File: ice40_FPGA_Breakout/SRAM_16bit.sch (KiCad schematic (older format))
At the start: 0 parts

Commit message: Added SO-DIMM header, ice40 IO and FTDI power
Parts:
- added C? (x3): C, symbol C
- added R? (x4): 10K, symbol R
- added U? (x3): iCE40HX8_CT256, symbol iCE40HX8_CT256
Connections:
- new net 3V3_REF_IN: C?.1, C?.1, C?.1, R?.1, R?.1, R?.1, R?.1, U?.N13 (VCC_SPI)
- new net FPGA_SPI_CLK: R?.2, U?.R11 (IOB_107_SCK)
- new net FPGA_SPI_CSN: R?.2, U?.R12 (IOB_108_SS)
- new net FPGA_SPI_SDI: R?.2, U?.P11 (IOB_106_SDI)
- new net FPGA_SPI_SDO: R?.2, U?.P12 (IOB_105_SDO)
- new net GND: C?.2, C?.2, C?.2
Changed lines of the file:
@@
 $Descr A4 11693 8268
 encoding utf-8
-Sheet 1 7
+Sheet 3 7
 Title ""
 Date ""
@@
 Comment4 ""
 $EndDescr
+$Comp
+L iCE40HX8_CT256 U?
+U 6 1 5A3EF3FF
+P 8250 5550
+AR Path="/5A0778ED/5A3EF3FF" Ref="U?"  Part="6"
+AR Path="/5A07796D/5A3EF3FF" Ref="U?"  Part="6"
+F 0 "U?" H 8350 5650 60  0000 C CNN
+F 1 "iCE40HX8_CT256" H 8950 5500 60  0000 C CNN
+F 2 "" H 8250 5550 60  0001 C CNN
+F 3 "" H 8250 5550 60  0001 C CNN
+	6    8250 5550
+	1    0    0    -1
+$EndComp
+Text HLabel 7450 5700 0    60   Input ~ 0
+FPGA_SPI_SDO
+Text HLabel 7450 5800 0    60   Input ~ 0
+FPGA_SPI_SDI
+Text HLabel 7450 5900 0    60   Input ~ 0
+FPGA_SPI_CLK
+Text HLabel 10400 5700 2    60   Input ~ 0
+FPGA_SPI_CSN
+Wire Wire Line
+	9900 5800 10050 5800
+Wire Wire Line
+	10050 5800 10250 5800
+$Comp
+L iCE40HX8_CT256 U?
+U 2 1 5A3F10D7
+P 2200 650
+F 0 "U?" H 2300 750 60  0000 C CNN
+F 1 "iCE40HX8_CT256" H 2900 550 60  0000 C CNN
+F 2 "" H 2200 650 60  0001 C CNN
+F 3 "" H 2200 650 60  0001 C CNN
+	2    2200 650
+	1    0    0    -1
+$EndComp
+$Comp
+L iCE40HX8_CT256 U?
+U 3 1 5A3F1322
+P 2200 4300
+F 0 "U?" H 2300 4400 60  0000 C CNN
+F 1 "iCE40HX8_CT256" H 2900 4200 60  0000 C CNN
+F 2 "" H 2200 4300 60  0001 C CNN
+F 3 "" H 2200 4300 60  0001 C CNN
+	3    2200 4300
+	1    0    0    -1
+$EndComp
+Wire Wire Line
+	7450 5700 7600 5700
+Wire Wire Line
+	7600 5700 8050 5700
+Wire Wire Line
+	7450 5800 7750 5800
+Wire Wire Line
+	7750 5800 8050 5800
+Wire Wire Line
+	7450 5900 7900 5900
+Wire Wire Line
+	7900 5900 8050 5900
+Wire Wire Line
+	9900 5700 10050 5700
+Wire Wire Line
+	10050 5700 10400 5700
+$Comp
+L R R?
+U 1 1 5A3F7BB8
+P 7750 5400
+F 0 "R?" V 7830 5400 50  0000 C CNN
+F 1 "10K" V 7750 5400 50  0000 C CNN
+F 2 "" V 7680 5400 50  0001 C CNN
+F 3 "" H 7750 5400 50  0001 C CNN
+	1    7750 5400
+	1    0    0    -1
+$EndComp
+$Comp
+L R R?
+U 1 1 5A3F7C81
+P 7900 5400
+F 0 "R?" V 7980 5400 50  0000 C CNN
+F 1 "10K" V 7900 5400 50  0000 C CNN
+F 2 "" V 7830 5400 50  0001 C CNN
+F 3 "" H 7900 5400 50  0001 C CNN
+	1    7900 5400
+	1    0    0    -1
+$EndComp
+$Comp
+L R R?
+U 1 1 5A3F7CA8
+P 7600 5400
+F 0 "R?" V 7680 5400 50  0000 C CNN
+F 1 "10K" V 7600 5400 50  0000 C CNN
+F 2 "" V 7530 5400 50  0001 C CNN
+F 3 "" H 7600 5400 50  0001 C CNN
+	1    7600 5400
+	1    0    0    -1
+$EndComp
+Wire Wire Line
+	7600 5550 7600 5700
+Connection ~ 7600 5700
+Wire Wire Line
+	7750 5550 7750 5800
+Connection ~ 7750 5800
+Wire Wire Line
+	7900 5550 7900 5900
+Connection ~ 7900 5900
+$Comp
+L R R?
+U 1 1 5A3F7DCD
+P 10050 5400
+F 0 "R?" V 10130 5400 50  0000 C CNN
+F 1 "10K" V 10050 5400 50  0000 C CNN
+F 2 "" V 9980 5400 50  0001 C CNN
+F 3 "" H 10050 5400 50  0001 C CNN
+	1    10050 5400
+	1    0    0    -1
+$EndComp
+Wire Wire Line
+	10050 5550 10050 5700
+Connection ~ 10050 5700
+Wire Wire Line
+	7600 5250 7600 5150
+Wire Wire Line
+	7750 5250 7750 5150
+Wire Wire Line
+	7900 5150 7900 5250
+Wire Wire Line
+	7600 5150 7750 5150
+Wire Wire Line
+	7750 5150 7900 5150
+Wire Wire Line
+	7900 5150 10050 5150
+Wire Wire Line
+	10050 5150 10250 5150
+Wire Wire Line
+	10250 5150 10400 5150
+Wire Wire Line
+	10400 5150 10650 5150
+Wire Wire Line
+	10650 5150 10750 5150
+Connection ~ 7750 5150
+Connection ~ 10050 5150
+Connection ~ 7900 5150
+Wire Wire Line
+	10050 5150 10050 5250
+$Comp
+L C C?
+U 1 1 5A3F8150
+P 10050 6050
+F 0 "C?" H 10075 6150 50  0000 L CNN
+F 1 "C" H 10075 5950 50  0000 L CNN
+F 2 "" H 10088 5900 50  0001 C CNN
+F 3 "" H 10050 6050 50  0001 C CNN
+	1    10050 6050
+	1    0    0    -1
+$EndComp
+Wire Wire Line
+	10050 5900 10050 5800
+Connection ~ 10050 5800
+Wire Wire Line
+	10050 6200 10050 6250
+$Comp
+L GND #PWR?
+U 1 1 5A3F82B7
+P 10050 6250
+F 0 "#PWR?" H 10050 6000 50  0001 C CNN
+F 1 "GND" H 10050 6100 50  0000 C CNN
+F 2 "" H 10050 6250 50  0001 C CNN
+F 3 "" H 10050 6250 50  0001 C CNN
+	1    10050 6250
+	1    0    0    -1
+$EndComp
+Wire Wire Line
+	10250 5800 10250 5150
+Connection ~ 10250 5150
+$Comp
+L C C?
+U 1 1 5A42CA88
+P 10400 5350
+F 0 "C?" H 10425 5450 50  0000 L CNN
+F 1 "C" H 10425 5250 50  0000 L CNN
+F 2 "" H 10438 5200 50  0001 C CNN
+F 3 "" H 10400 5350 50  0001 C CNN
+	1    10400 5350
+	1    0    0    -1
+$EndComp
+$Comp
+L C C?
+U 1 1 5A42CAE0
+P 10650 5350
+F 0 "C?" H 10675 5450 50  0000 L CNN
+F 1 "C" H 10675 5250 50  0000 L CNN
+F 2 "" H 10688 5200 50  0001 C CNN
+F 3 "" H 10650 5350 50  0001 C CNN
+	1    10650 5350
+	1    0    0    -1
+$EndComp
+Wire Wire Line
+	10400 5500 10400 5550
+Wire Wire Line
+	10400 5550 10650 5550
+Wire Wire Line
+	10650 5550 10700 5550
+Wire Wire Line
+	10650 5550 10650 5500
+Wire Wire Line
+	10400 5200 10400 5150
+Connection ~ 10400 5150
+Wire Wire Line
+	10650 5200 10650 5150
+Connection ~ 10650 5150
+$Comp
+L GND #PWR?
+U 1 1 5A42CBA9
+P 10700 5550
+F 0 "#PWR?" H 10700 5300 50  0001 C CNN
+F 1 "GND" H 10800 5550 50  0000 C CNN
+F 2 "" H 10700 5550 50  0001 C CNN
+F 3 "" H 10700 5550 50  0001 C CNN
+	1    10700 5550
+	1    0    0    -1
+$EndComp
+Connection ~ 10650 5550
+Text HLabel 10750 5150 2    39   Input ~ 0
+3V3_REF_IN
 $EndSCHEMATC

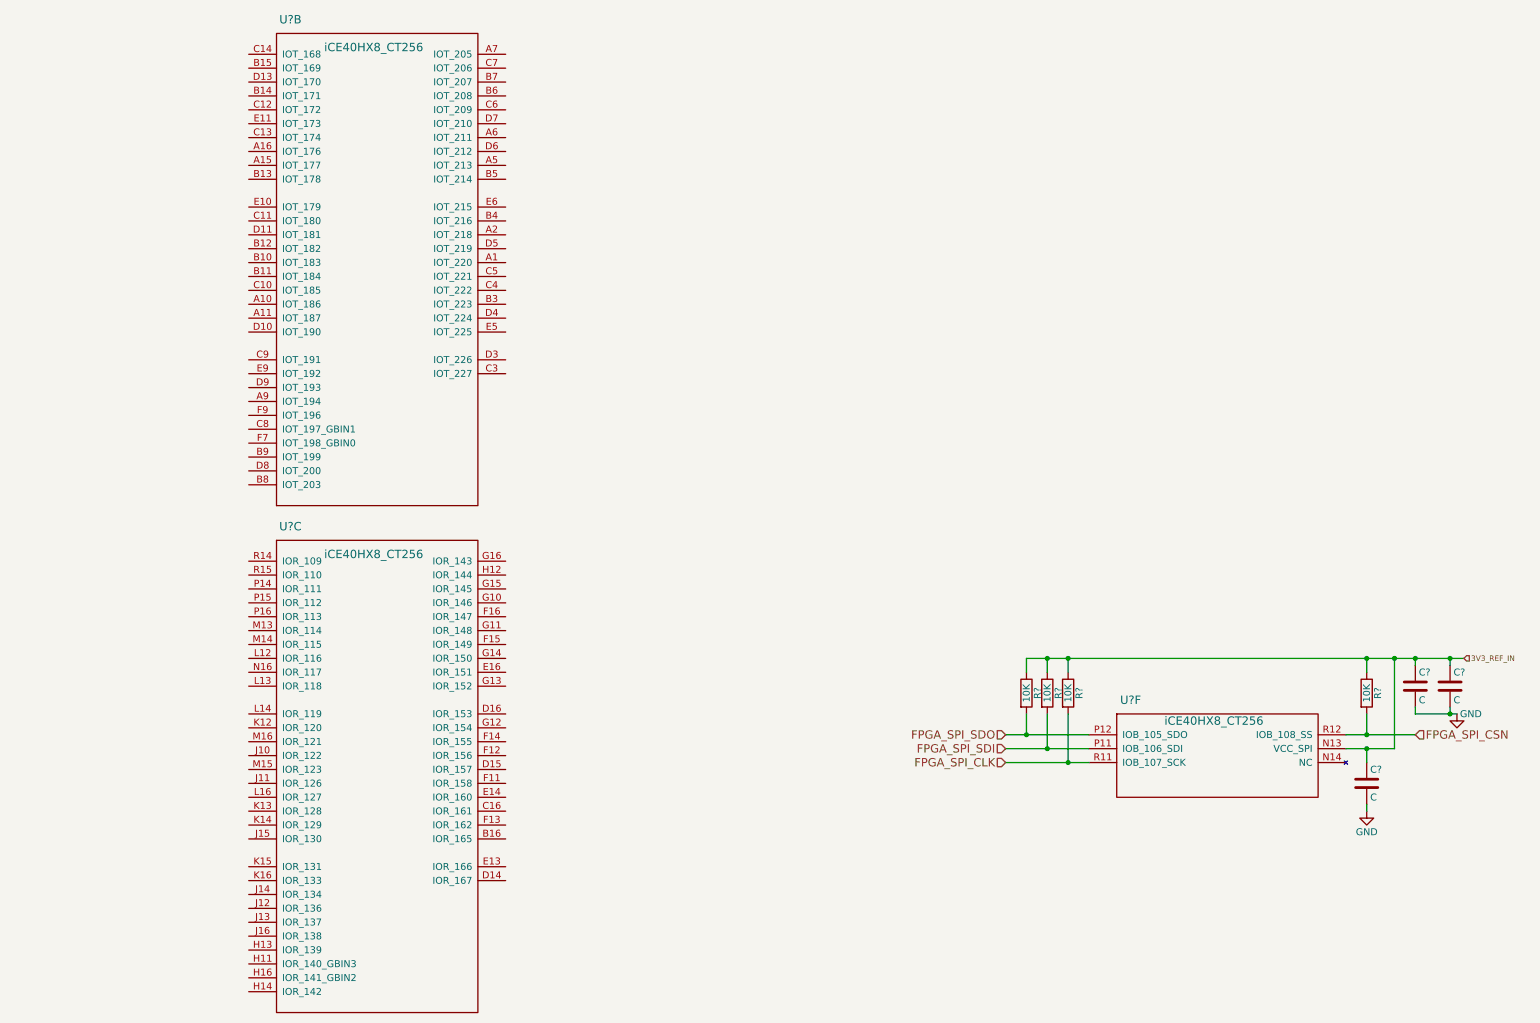
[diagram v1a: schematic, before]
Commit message: Add SPI EEPROM logic for SPI switching
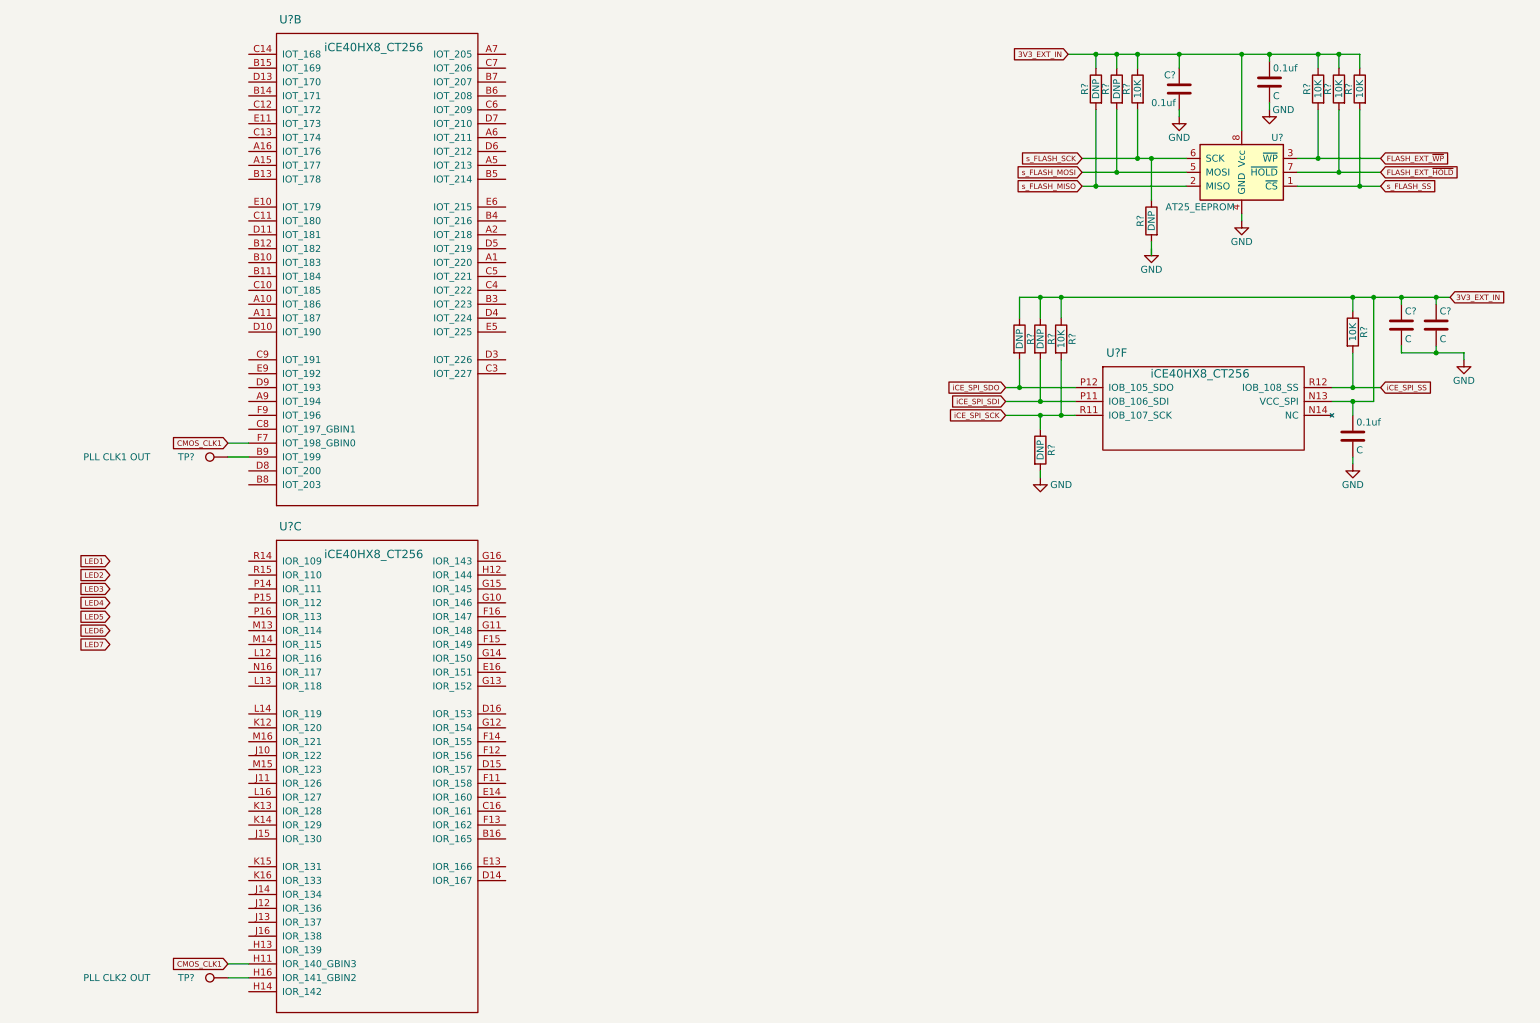
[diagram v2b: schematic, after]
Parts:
- added 0.1uf: C, symbol C
- added C?: 0.1uf, symbol C
- added R? (x4): 10K, symbol R
- added R? (x4): DNP, symbol R
- added TP?: PLL CLK1 OUT, symbol Test_Point
- added TP?: PLL CLK2 OUT, symbol Test_Point
- added U?: AT25_EEPROM, symbol AT25_EEPROM
- R? (x2): value 10K -> DNP
- gave numbers to parts that had none: 1
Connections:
- net GND: now also 0.1uf.2, C?.2, R?.2, U?.4 (GND)
- net at U?.B9 (IOT_199): now also TP?.1
- net CMOS_CLK1: now reaches U?.F7 (IOT_198_GBIN0)
- net CMOS_CLK1: now also U?.H11 (IOR_140_GBIN3)
- net at U?.H16 (IOR_141_GBIN2): now also TP?.1
- net 3V3_REF_IN renamed 3V3_EXT_IN
- net 3V3_EXT_IN: now also 0.1uf.1, C?.1, R?.1, R?.1, R?.1, R?.1, R?.1, R?.1, U?.8 (Vcc)
- net FPGA_SPI_CLK renamed iCE_SPI_SCK
- net iCE_SPI_SCK: now also R?.1
- net FPGA_SPI_CSN renamed iCE_SPI_SS
- net FPGA_SPI_SDI renamed iCE_SPI_SDI
- net FPGA_SPI_SDO renamed iCE_SPI_SDO
- new net FLASH_EXT_~HOLD: R?.2, U?.7 (~HOLD)
- new net FLASH_EXT_~WP: R?.2, U?.3 (~WP)
- new net s_FLASH_MISO: R?.2, U?.2 (MISO)
- new net s_FLASH_MOSI: R?.2, U?.5 (MOSI)
- new net s_FLASH_SCK: R?.1, R?.2, U?.6 (SCK)
- new net s_FLASH_SS: R?.2, U?.1 (~CS)
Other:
- moved on the sheet: 0.1uf, C?, R?, U?F

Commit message: global nets changed to hierarchy net, interconnects updated
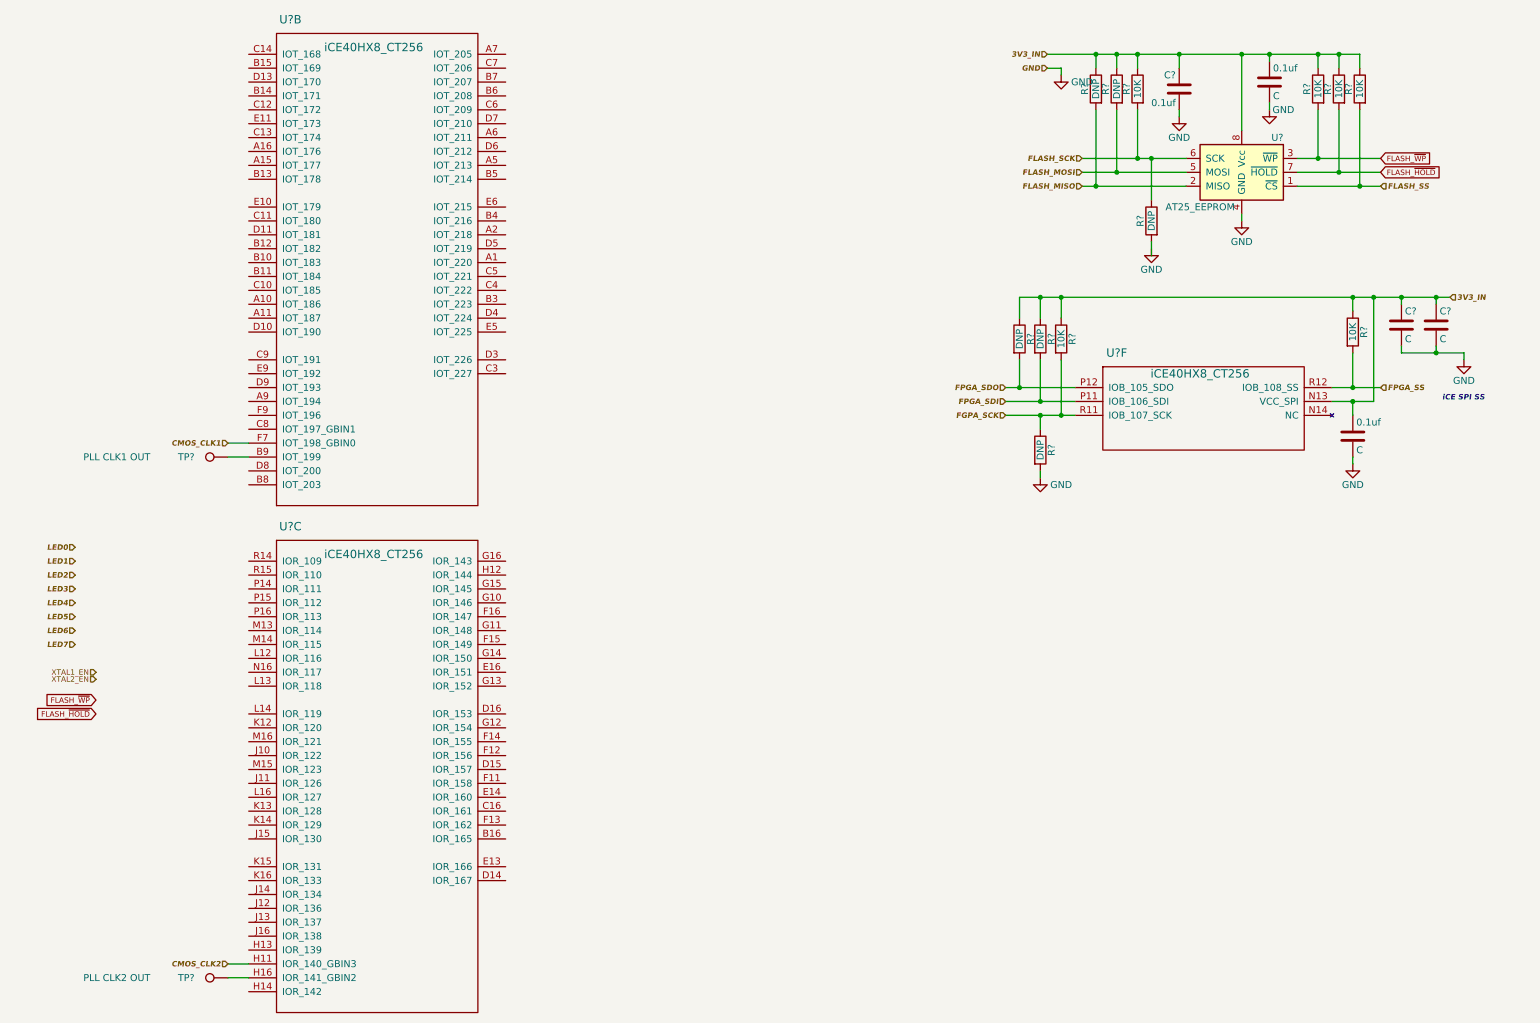
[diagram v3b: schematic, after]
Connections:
- net CMOS_CLK1: no longer U?.H11 (IOR_140_GBIN3)
- net 3V3_EXT_IN renamed 3V3_IN
- net FLASH_EXT_~HOLD renamed FLASH_~HOLD
- net FLASH_EXT_~WP renamed FLASH_~WP
- net iCE_SPI_SCK renamed FGPA_SCK
- net iCE_SPI_SDI renamed FPGA_SDI
- net iCE_SPI_SDO renamed FPGA_SDO
- net iCE_SPI_SS renamed FPGA_SS
- net s_FLASH_MISO renamed FLASH_MISO
- net s_FLASH_MOSI renamed FLASH_MOSI
- net s_FLASH_SCK renamed FLASH_SCK
- net s_FLASH_SS renamed FLASH_SS
- new net CMOS_CLK2: U?.H11 (IOR_140_GBIN3)
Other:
- note added: "iCE SPI SS"
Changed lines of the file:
@@
 $EndComp
 $Comp
-L GND #PWR?
+L GND #PWR011
 U 1 1 5A3F82B7
 P 9950 3750
-F 0 "#PWR?" H 9950 3500 50  0001 C CNN
+F 0 "#PWR011" H 9950 3500 50  0001 C CNN
 F 1 "GND" H 9950 3600 50  0000 C CNN
 F 2 "" H 9950 3750 50  0001 C CNN
@@
 	-1   0    0    -1
 $EndComp
-Text GLabel 7900 800  0    39   Input ~ 0
-3V3_EXT_IN
-Text GLabel 10150 1550 2    39   Input ~ 0
-FLASH_EXT_~WP
-Text GLabel 10150 1650 2    39   Input ~ 0
-FLASH_EXT_~HOLD
-$Comp
-L GND #PWR?
+$Comp
+L GND #PWR012
 U 1 1 5A2D962F
 P 9150 2000
-F 0 "#PWR?" H 9150 1750 50  0001 C CNN
+F 0 "#PWR012" H 9150 1750 50  0001 C CNN
 F 1 "GND" H 9150 1850 50  0000 C CNN
 F 2 "" H 9150 2000 50  0001 C CNN
@@
 $EndComp
 $Comp
-L GND #PWR?
+L GND #PWR013
 U 1 1 5A2D9808
 P 8700 1250
-F 0 "#PWR?" H 8700 1000 50  0001 C CNN
+F 0 "#PWR013" H 8700 1000 50  0001 C CNN
 F 1 "GND" H 8700 1100 50  0000 C CNN
 F 2 "" H 8700 1250 50  0001 C CNN
@@
 $EndComp
 $Comp
-L GND #PWR?
+L GND #PWR014
 U 1 1 5A2DC454
 P 7700 3850
-F 0 "#PWR?" H 7700 3600 50  0001 C CNN
+F 0 "#PWR014" H 7700 3600 50  0001 C CNN
 F 1 "GND" H 7850 3800 50  0000 C CNN
 F 2 "" H 7700 3850 50  0001 C CNN
@@
 $EndComp
 $Comp
-L GND #PWR?
+L GND #PWR015
 U 1 1 5A2DC8C5
 P 8500 2200
-F 0 "#PWR?" H 8500 1950 50  0001 C CNN
+F 0 "#PWR015" H 8500 1950 50  0001 C CNN
 F 1 "GND" H 8500 2050 50  0000 C CNN
 F 2 "" H 8500 2200 50  0001 C CNN
@@
 	-1   0    0    -1
 $EndComp
-Text GLabel 1850 3600 0    39   Input ~ 0
-CMOS_CLK1
-Text GLabel 10650 2550 2    39   Input ~ 0
-3V3_EXT_IN
-Text GLabel 7450 3200 0    39   Input ~ 0
-iCE_SPI_SDO
-Text GLabel 7450 3300 0    39   Input ~ 0
-iCE_SPI_SDI
-Text GLabel 7450 3400 0    39   Input ~ 0
-iCE_SPI_SCK
-Text GLabel 10150 3200 2    39   Input ~ 0
-iCE_SPI_SS
-Text GLabel 8000 1550 0    39   Input ~ 0
-s_FLASH_SCK
-Text GLabel 8000 1650 0    39   Input ~ 0
-s_FLASH_MOSI
-Text GLabel 8000 1750 0    39   Input ~ 0
-s_FLASH_MISO
-Text GLabel 10150 1750 2    39   Input ~ 0
-s_FLASH_SS
 Wire Wire Line
 	9800 3300 10100 3300
@@
 	10000 800  10000 900
 Wire Wire Line
-	7900 800  10000 800
+	7750 800  10000 800
 Wire Wire Line
 	9850 800  9850 900
@@
 	7450 3200 7950 3200
 $Comp
-L GND #PWR?
+L GND #PWR016
 U 1 1 5A2E5ABD
 P 10750 3000
-F 0 "#PWR?" H 10750 2750 50  0001 C CNN
+F 0 "#PWR016" H 10750 2750 50  0001 C CNN
 F 1 "GND" H 10750 2850 50  0000 C CNN
 F 2 "" H 10750 3000 50  0001 C CNN
@@
 Wire Wire Line
 	10750 2950 10750 3000
-Text GLabel 1850 7350 0    39   Input ~ 0
-CMOS_CLK1
 Wire Wire Line
 	1850 7350 2000 7350
@@
 $EndComp
 $Comp
-L GND #PWR?
+L GND #PWR017
 U 1 1 5A2FB32F
 P 9350 1200
-F 0 "#PWR?" H 9350 950 50  0001 C CNN
+F 0 "#PWR017" H 9350 950 50  0001 C CNN
 F 1 "GND" H 9250 1200 50  0000 C CNN
 F 2 "" H 9350 1200 50  0001 C CNN
@@
 	9350 850  9350 800
 Connection ~ 9350 800
-Text GLabel 1000 4450 0    39   Input ~ 0
+Text HLabel 7750 800  0    39   Input Italic 8
+3V3_IN
+Text HLabel 8000 1550 0    39   Input Italic 8
+FLASH_SCK
+Text HLabel 8000 1650 0    39   Input Italic 8
+FLASH_MOSI
+Text HLabel 8000 1750 0    39   Input Italic 8
+FLASH_MISO
+Text HLabel 10150 1750 2    39   Input Italic 8
+FLASH_SS
+Text HLabel 10650 2550 2    39   Input Italic 8
+3V3_IN
+Text HLabel 7450 3200 0    39   Input Italic 8
+FPGA_SDO
+Text HLabel 7450 3300 0    39   Input Italic 8
+FPGA_SDI
+Text HLabel 7450 3400 0    39   Input Italic 8
+FGPA_SCK
+Text HLabel 10150 3200 2    39   Input Italic 8
+FPGA_SS
+Text Notes 10900 3300 2    39   Italic 8
+iCE SPI SS
+Text HLabel 1850 3600 0    39   Input Italic 8
+CMOS_CLK1
+Text HLabel 1850 7350 0    39   Input Italic 8
+CMOS_CLK2
+Text HLabel 750  4450 0    39   Input Italic 8
 LED1
-Text GLabel 1000 4550 0    39   Input ~ 0
+Text HLabel 750  4550 0    39   Input Italic 8
 LED2
-Text GLabel 1000 4650 0    39   Input ~ 0
+Text HLabel 750  4650 0    39   Input Italic 8
 LED3
-Text GLabel 1000 4750 0    39   Input ~ 0
+Text HLabel 750  4750 0    39   Input Italic 8
 LED4
-Text GLabel 1000 4850 0    39   Input ~ 0
+Text HLabel 750  4850 0    39   Input Italic 8
 LED5
-Text GLabel 1000 4950 0    39   Input ~ 0
+Text HLabel 750  4950 0    39   Input Italic 8
 LED6
-Text GLabel 1000 5050 0    39   Input ~ 0
+Text HLabel 750  5050 0    39   Input Italic 8
 LED7
+Text HLabel 750  4350 0    39   Input Italic 8
+LED0
+$Comp
+L GND #PWR018
+U 1 1 5A4230FF
+P 7850 950
+F 0 "#PWR018" H 7850 700 50  0001 C CNN
+F 1 "GND" H 8000 900 50  0000 C CNN
+F 2 "" H 7850 950 50  0001 C CNN
+F 3 "" H 7850 950 50  0001 C CNN
+	1    7850 950
+	1    0    0    -1
+$EndComp
+Text HLabel 7750 900  0    39   Input Italic 8
+GND
+Wire Wire Line
+	7750 900  7850 900
+Wire Wire Line
+	7850 900  7850 950
+Text HLabel 900  5250 0    39   Input ~ 0
+XTAL1_EN
+Text HLabel 900  5300 0    39   Input ~ 0
+XTAL2_EN
+Text GLabel 10150 1550 2    39   Input ~ 0
+FLASH_~WP
+Text GLabel 10150 1650 2    39   Input ~ 0
+FLASH_~HOLD
+Text GLabel 900  5450 0    39   Input ~ 0
+FLASH_~WP
+Text GLabel 900  5550 0    39   Input ~ 0
+FLASH_~HOLD
 $EndSCHEMATC
